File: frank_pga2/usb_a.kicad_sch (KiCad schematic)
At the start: 38 parts, among them J7 SS-52100-004, J8 SS-52100-004, U10 CH217K, U11 CH217K, U12 CH217K, U13 CH217K, U19 USBLC6-2SC6, U20 USBLC6-2SC6, U21 USBLC6-2SC6, U22 USBLC6-2SC6, U9 MW7211A

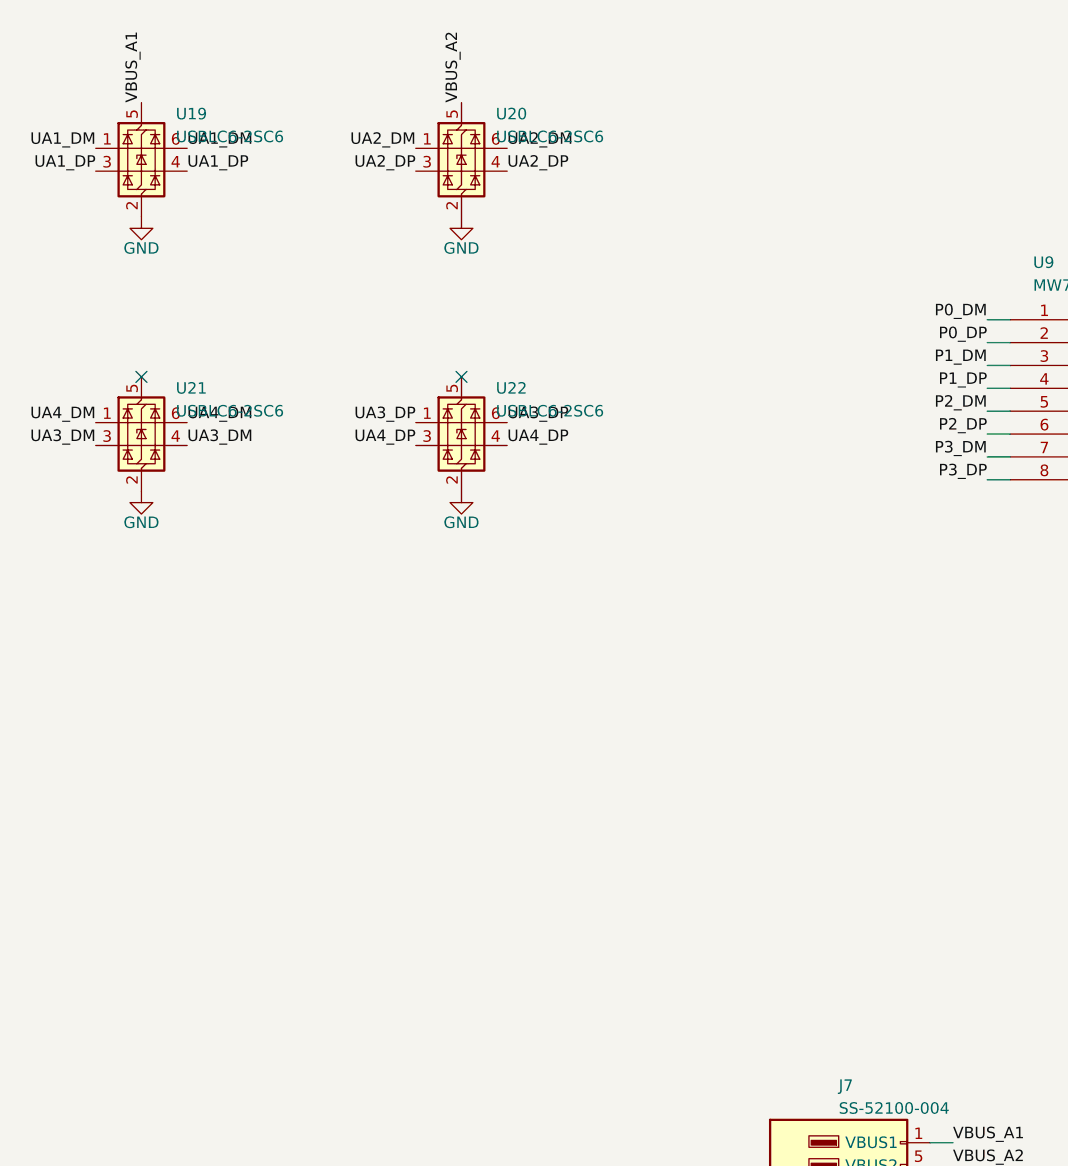
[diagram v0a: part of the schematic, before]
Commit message: fix: frank_pga2 1.00 - silkscreen labels, TP7 on the back, release refresh
- Reference labels re-placed on true geometry: 0.15 mm from the part's
  pads/silk/fab on one of four sides (rotated on left/right), clear of
  other parts, labels, via drills and the edge. Fixes D2 sitting on U3,
  uneven U10/U13/U7 gaps from pin-1 markers, C10/C11/R31/R16/R17 crowding.
  C17/C52/C56 shown again; R28 hidden (no room after the via moves)
- TP7 (VIN_PROT) moved to the back like every other test point, fed
  through a via pair from the front VIN_PROT pour
- Routing touch-ups
- Release 1.00 regenerated: gerbers, schematics, assembly PDF, iBOM
  (ERC 0/0, DRC 0 violations, 0 unconnected, 0 parity)
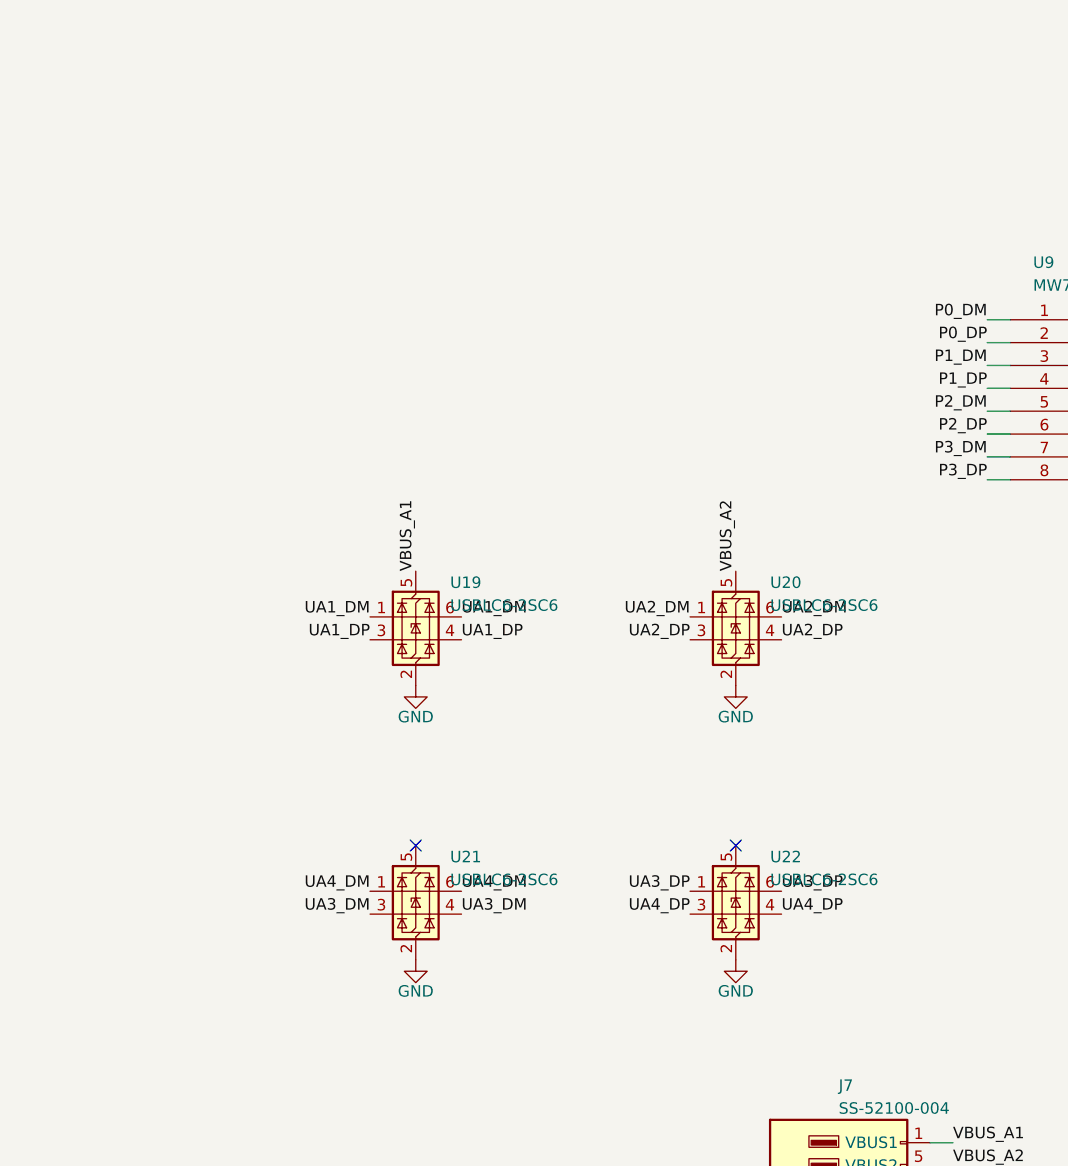
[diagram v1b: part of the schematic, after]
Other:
- moved on the sheet: U19, U20, U21, U22
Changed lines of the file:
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@@
 	)
 	(no_connect
-		(at 50.8 66.04)
+		(at 81.28 118.11)
 	)
 	(no_connect
@@
 	)
 	(no_connect
-		(at 86.36 66.04)
+		(at 116.84 118.11)
 	)
 	(wire
@@
 	)
 	(label "UA3_DM"
-		(at 55.88 73.66 0)
+		(at 86.36 125.73 0)
 		(effects
 			(font
@@
 	)
 	(label "UA3_DM"
-		(at 45.72 73.66 180)
+		(at 76.2 125.73 180)
 		(effects
 			(font
@@
 	)
 	(label "UA1_DM"
-		(at 55.88 40.64 0)
+		(at 86.36 92.71 0)
 		(effects
 			(font
@@
 	)
 	(label "UA4_DP"
-		(at 81.28 73.66 180)
+		(at 111.76 125.73 180)
 		(effects
 			(font
@@
 	)
 	(label "UA2_DP"
-		(at 81.28 43.18 180)
+		(at 111.76 95.25 180)
 		(effects
 			(font
@@
 	)
 	(label "UA1_DM"
-		(at 45.72 40.64 180)
+		(at 76.2 92.71 180)
 		(effects
 			(font
@@
 	)
 	(label "UA1_DP"
-		(at 45.72 43.18 180)
+		(at 76.2 95.25 180)
 		(effects
 			(font
@@
 	)
 	(label "UA4_DM"
-		(at 45.72 71.12 180)
+		(at 76.2 123.19 180)
 		(effects
 			(font
@@
 	)
 	(label "UA1_DP"
-		(at 55.88 43.18 0)
+		(at 86.36 95.25 0)
 		(effects
 			(font
@@
 	)
 	(label "VBUS_A2"
-		(at 86.36 35.56 90)
+		(at 116.84 87.63 90)
 		(effects
 			(font
@@
 	)
 	(label "UA4_DM"
-		(at 55.88 71.12 0)
+		(at 86.36 123.19 0)
 		(effects
 			(font
@@
 	)
 	(label "UA2_DM"
-		(at 91.44 40.64 0)
+		(at 121.92 92.71 0)
 		(effects
 			(font
@@
 	)
 	(label "UA4_DP"
-		(at 91.44 73.66 0)
+		(at 121.92 125.73 0)
 		(effects
 			(font
@@
 	)
 	(label "UA2_DM"
-		(at 81.28 40.64 180)
+		(at 111.76 92.71 180)
 		(effects
 			(font
@@
 	)
 	(label "UA3_DP"
-		(at 91.44 71.12 0)
+		(at 121.92 123.19 0)
 		(effects
 			(font
@@
 	)
 	(label "VBUS_A1"
-		(at 50.8 35.56 90)
+		(at 81.28 87.63 90)
 		(effects
 			(font
@@
 	)
 	(label "UA2_DP"
-		(at 91.44 43.18 0)
+		(at 121.92 95.25 0)
 		(effects
 			(font
@@
 	)
 	(label "UA3_DP"
-		(at 81.28 71.12 180)
+		(at 111.76 123.19 180)
 		(effects
 			(font
@@
 	(symbol
 		(lib_id "FRANK:GND")
-		(at 50.8 48.26 0)
+		(at 81.28 100.33 0)
 		(unit 1)
 		(body_style 1)
@@
 		(dnp no)
 		(property "Reference" "#PWR222"
-			(at 50.8 53.26 0)
+			(at 81.28 105.33 0)
 			(hide yes)
 			(show_name no)
@@
 		)
 		(property "Value" "GND"
-			(at 50.8 51.76 0)
+			(at 81.28 103.83 0)
 			(show_name no)
 			(do_not_autoplace no)
@@
 		)
 		(property "Footprint" ""
-			(at 50.8 48.26 0)
+			(at 81.28 100.33 0)
 			(hide yes)
 			(show_name no)
@@
 		)
 		(property "Datasheet" ""
-			(at 50.8 48.26 0)
+			(at 81.28 100.33 0)
 			(hide yes)
 			(show_name no)
@@
 		)
 		(property "Description" ""
-			(at 50.8 48.26 0)
+			(at 81.28 100.33 0)
 			(show_name no)
 			(do_not_autoplace no)
@@
 	(symbol
 		(lib_id "FRANK:USBLC6-2SC6")
-		(at 50.8 71.12 0)
+		(at 81.28 123.19 0)
 		(unit 1)
 		(body_style 1)
@@
 		(dnp no)
 		(property "Reference" "U21"
-			(at 54.61 67.31 0)
+			(at 85.09 119.38 0)
 			(show_name no)
 			(do_not_autoplace no)
@@
 		)
 		(property "Value" "USBLC6-2SC6"
-			(at 54.61 69.85 0)
+			(at 85.09 121.92 0)
 			(show_name no)
 			(do_not_autoplace no)
@@
 		)
 		(property "Footprint" "FRANK:SOT-23-6"
-			(at 50.8 71.12 0)
+			(at 81.28 123.19 0)
 			(hide yes)
 			(show_name no)
@@
 		)
 		(property "Datasheet" ""
-			(at 50.8 71.12 0)
+			(at 81.28 123.19 0)
 			(hide yes)
 			(show_name no)
@@
 		)
 		(property "Description" ""
-			(at 50.8 71.12 0)
+			(at 81.28 123.19 0)
 			(show_name no)
 			(do_not_autoplace no)
@@
 	(symbol
 		(lib_id "FRANK:GND")
-		(at 50.8 78.74 0)
+		(at 81.28 130.81 0)
 		(unit 1)
 		(body_style 1)
@@
 		(dnp no)
 		(property "Reference" "#PWR224"
-			(at 50.8 83.74 0)
+			(at 81.28 135.81 0)
 			(hide yes)
 			(show_name no)
@@
 		)
 		(property "Value" "GND"
-			(at 50.8 82.24 0)
+			(at 81.28 134.31 0)
 			(show_name no)
 			(do_not_autoplace no)
@@
 		)
 		(property "Footprint" ""
-			(at 50.8 78.74 0)
+			(at 81.28 130.81 0)
 			(hide yes)
 			(show_name no)
@@
 		)
 		(property "Datasheet" ""
-			(at 50.8 78.74 0)
+			(at 81.28 130.81 0)
 			(hide yes)
 			(show_name no)
@@
 		)
 		(property "Description" ""
-			(at 50.8 78.74 0)
+			(at 81.28 130.81 0)
 			(show_name no)
 			(do_not_autoplace no)
@@
 	(symbol
 		(lib_id "FRANK:USBLC6-2SC6")
-		(at 50.8 40.64 0)
+		(at 81.28 92.71 0)
 		(unit 1)
 		(body_style 1)
@@
 		(dnp no)
 		(property "Reference" "U19"
-			(at 54.61 36.83 0)
+			(at 85.09 88.9 0)
 			(show_name no)
 			(do_not_autoplace no)
@@
 		)
 		(property "Value" "USBLC6-2SC6"
-			(at 54.61 39.37 0)
+			(at 85.09 91.44 0)
 			(show_name no)
 			(do_not_autoplace no)
@@
 		)
 		(property "Footprint" "FRANK:SOT-23-6"
-			(at 50.8 40.64 0)
+			(at 81.28 92.71 0)
 			(hide yes)
 			(show_name no)
@@
 		)
 		(property "Datasheet" ""
-			(at 50.8 40.64 0)
+			(at 81.28 92.71 0)
 			(hide yes)
 			(show_name no)
@@
 		)
 		(property "Description" ""
-			(at 50.8 40.64 0)
+			(at 81.28 92.71 0)
 			(show_name no)
 			(do_not_autoplace no)
@@
 	(symbol
 		(lib_id "FRANK:GND")
-		(at 86.36 48.26 0)
+		(at 116.84 100.33 0)
 		(unit 1)
 		(body_style 1)
@@
 		(dnp no)
 		(property "Reference" "#PWR223"
-			(at 86.36 53.26 0)
+			(at 116.84 105.33 0)
 			(hide yes)
 			(show_name no)
@@
 		)
 		(property "Value" "GND"
-			(at 86.36 51.76 0)
+			(at 116.84 103.83 0)
 			(show_name no)
 			(do_not_autoplace no)
@@
 		)
 		(property "Footprint" ""
-			(at 86.36 48.26 0)
+			(at 116.84 100.33 0)
 			(hide yes)
 			(show_name no)
@@
 		)
 		(property "Datasheet" ""
-			(at 86.36 48.26 0)
+			(at 116.84 100.33 0)
 			(hide yes)
 			(show_name no)
@@
 		)
 		(property "Description" ""
-			(at 86.36 48.26 0)
+			(at 116.84 100.33 0)
 			(show_name no)
 			(do_not_autoplace no)
@@
 	(symbol
 		(lib_id "FRANK:GND")
-		(at 86.36 78.74 0)
+		(at 116.84 130.81 0)
 		(unit 1)
 		(body_style 1)
@@
 		(dnp no)
 		(property "Reference" "#PWR225"
-			(at 86.36 83.74 0)
+			(at 116.84 135.81 0)
 			(hide yes)
 			(show_name no)
@@
 		)
 		(property "Value" "GND"
-			(at 86.36 82.24 0)
+			(at 116.84 134.31 0)
 			(show_name no)
 			(do_not_autoplace no)
@@
 		)
 		(property "Footprint" ""
-			(at 86.36 78.74 0)
+			(at 116.84 130.81 0)
 			(hide yes)
 			(show_name no)
@@
 		)
 		(property "Datasheet" ""
-			(at 86.36 78.74 0)
+			(at 116.84 130.81 0)
 			(hide yes)
 			(show_name no)
@@
 		)
 		(property "Description" ""
-			(at 86.36 78.74 0)
+			(at 116.84 130.81 0)
 			(show_name no)
 			(do_not_autoplace no)
@@
 	(symbol
 		(lib_id "FRANK:USBLC6-2SC6")
-		(at 86.36 71.12 0)
+		(at 116.84 123.19 0)
 		(unit 1)
 		(body_style 1)
@@
 		(dnp no)
 		(property "Reference" "U22"
-			(at 90.17 67.31 0)
+			(at 120.65 119.38 0)
 			(show_name no)
 			(do_not_autoplace no)
@@
 		)
 		(property "Value" "USBLC6-2SC6"
-			(at 90.17 69.85 0)
+			(at 120.65 121.92 0)
 			(show_name no)
 			(do_not_autoplace no)
@@
 		)
 		(property "Footprint" "FRANK:SOT-23-6"
-			(at 86.36 71.12 0)
+			(at 116.84 123.19 0)
 			(hide yes)
 			(show_name no)
@@
 		)
 		(property "Datasheet" ""
-			(at 86.36 71.12 0)
+			(at 116.84 123.19 0)
 			(hide yes)
 			(show_name no)
@@
 		)
 		(property "Description" ""
-			(at 86.36 71.12 0)
+			(at 116.84 123.19 0)
 			(show_name no)
 			(do_not_autoplace no)
@@
 	(symbol
 		(lib_id "FRANK:USBLC6-2SC6")
-		(at 86.36 40.64 0)
+		(at 116.84 92.71 0)
 		(unit 1)
 		(body_style 1)
@@
 		(dnp no)
 		(property "Reference" "U20"
-			(at 90.17 36.83 0)
+			(at 120.65 88.9 0)
 			(show_name no)
 			(do_not_autoplace no)
@@
 		)
 		(property "Value" "USBLC6-2SC6"
-			(at 90.17 39.37 0)
+			(at 120.65 91.44 0)
 			(show_name no)
 			(do_not_autoplace no)
@@
 		)
 		(property "Footprint" "FRANK:SOT-23-6"
-			(at 86.36 40.64 0)
+			(at 116.84 92.71 0)
 			(hide yes)
 			(show_name no)
@@
 		)
 		(property "Datasheet" ""
-			(at 86.36 40.64 0)
+			(at 116.84 92.71 0)
 			(hide yes)
 			(show_name no)
@@
 		)
 		(property "Description" ""
-			(at 86.36 40.64 0)
+			(at 116.84 92.71 0)
 			(show_name no)
 			(do_not_autoplace no)
